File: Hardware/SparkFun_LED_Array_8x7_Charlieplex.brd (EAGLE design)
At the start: 27.9 x 43.2 mm, 76 parts

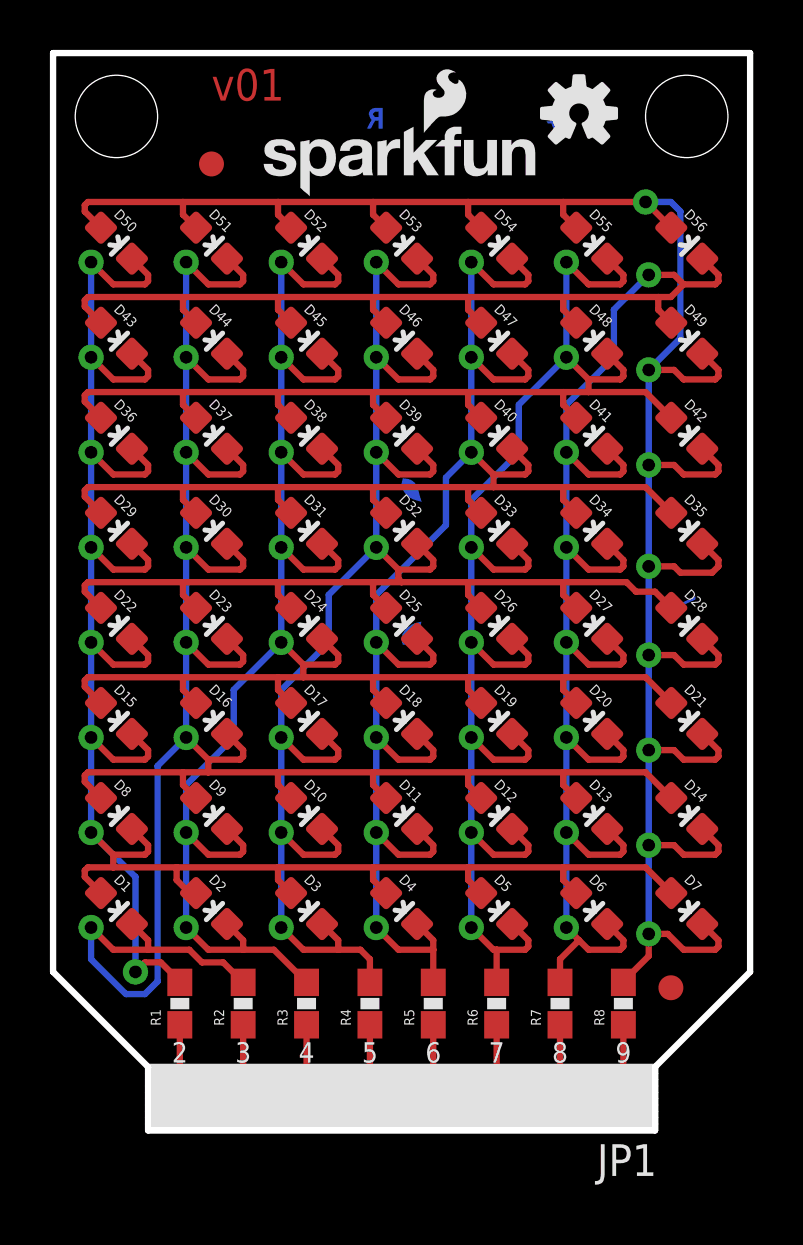
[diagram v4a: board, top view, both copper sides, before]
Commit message: Flipped all silk screen on bottom of board. Switched top and bottom silk pin numbers. Flipped order of pin numbers to line up with the Interactive Badge.
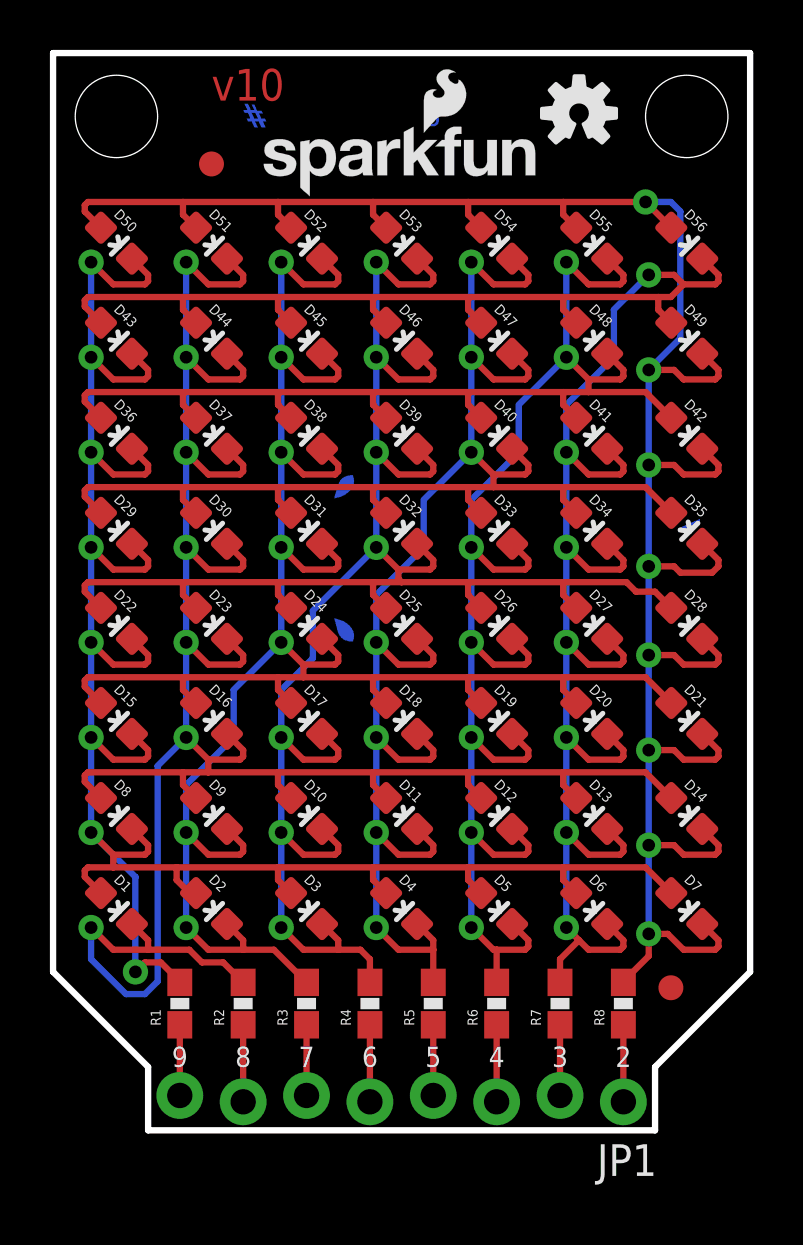
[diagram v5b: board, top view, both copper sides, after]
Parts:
- moved U$3 22.5 mm to (25.0, 11.9), turned to 90 degrees
- moved U$4 22.3 mm to (4.45, 15.7), turned to 90 degrees
- moved U$6 12.9 mm to (7.62, 41.1), turned to 180 degrees

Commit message: Changed pin numbers to letters (A-H). Changed revision to v11.
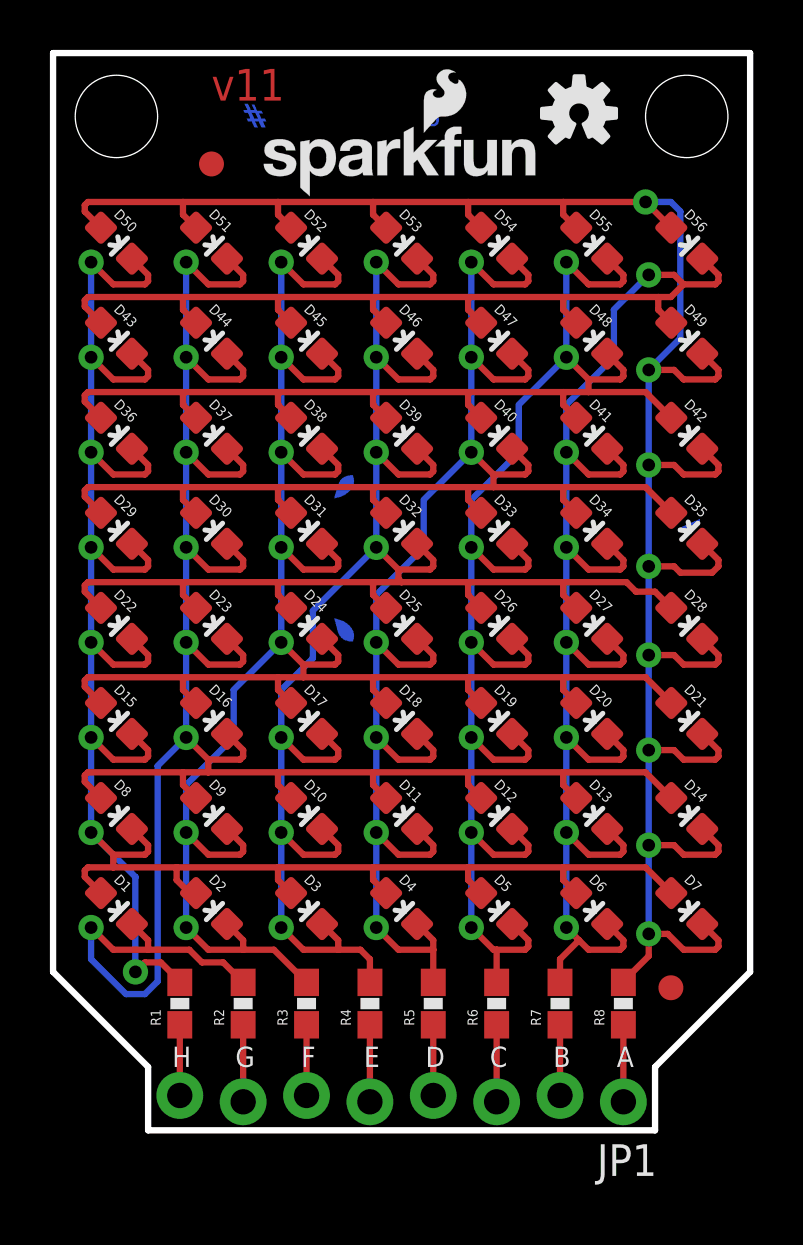
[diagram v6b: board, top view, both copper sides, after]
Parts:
- R1, R2, R3, R4, R5, R6, R7, R8: value 33 -> 82
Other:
- board text added: "A"
- board text added: "B"
- board text added: "C"
- board text added: "D"
- board text added: "E"
- board text added: "F"
- board text added: "G"
- board text added: "H"
- board text removed: "2"
- board text removed: "3"
- board text removed: "4"
- board text removed: "5"
- board text removed: "6"
- board text removed: "7"
- board text removed: "8"
- board text removed: "9"

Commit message: Swapped resistors for 82 Ohm. Made link and hashtag larger on silk.
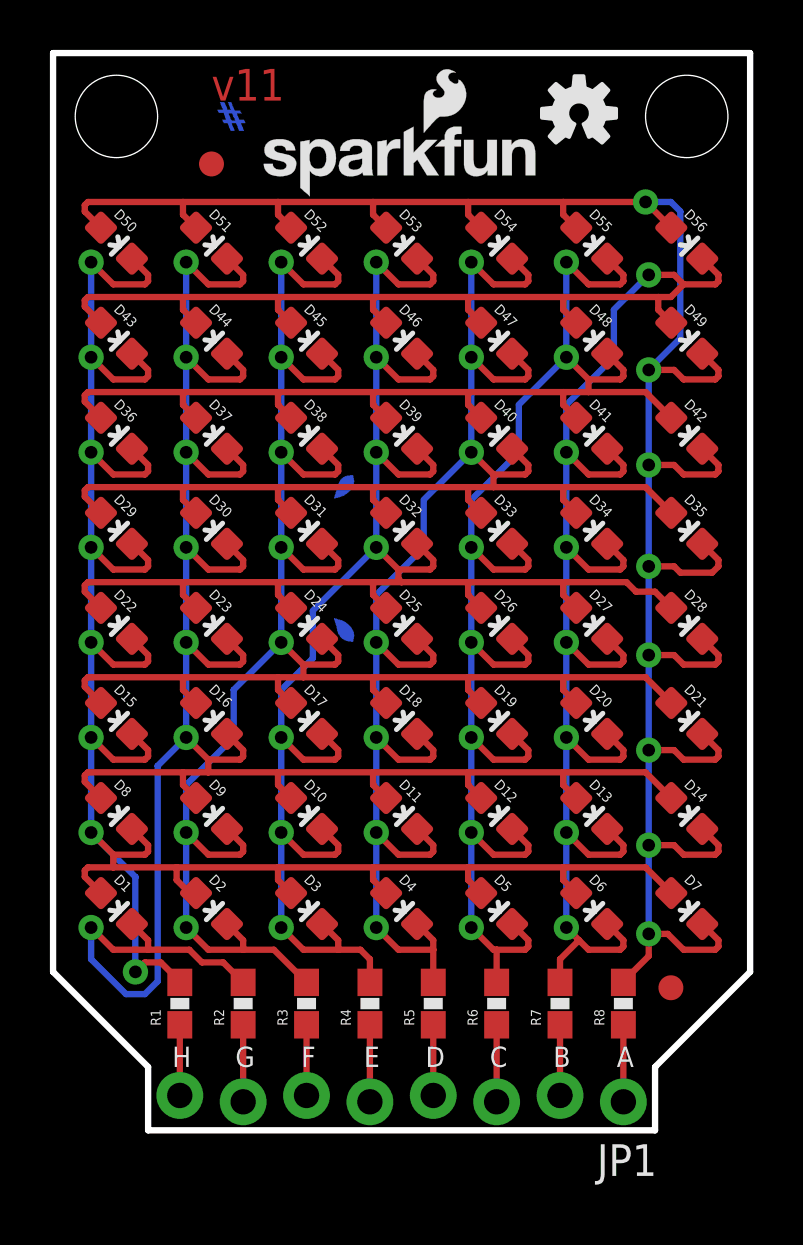
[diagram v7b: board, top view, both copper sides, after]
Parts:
- moved U$3 5.09 mm to (24.8, 6.86)
- moved U$6 1.04 mm to (6.58, 41.2)
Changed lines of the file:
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@@
 <setting verticaltext="up"/>
 </settings>
-<grid distance="0.01" unitdist="inch" unit="inch" style="dots" multiple="1" display="yes" altdistance="0.005" altunitdist="inch" altunit="inch"/>
+<grid distance="0.05" unitdist="inch" unit="inch" style="dots" multiple="1" display="yes" altdistance="0.005" altunitdist="inch" altunit="inch"/>
 <layers>
 <layer number="1" name="Top" color="4" fill="1" visible="yes" active="yes"/>
 <layer number="2" name="Route2" color="1" fill="3" visible="no" active="yes"/>
 <layer number="15" name="Route15" color="4" fill="6" visible="no" active="yes"/>
-<layer number="16" name="Bottom" color="1" fill="1" visible="no" active="yes"/>
+<layer number="16" name="Bottom" color="1" fill="1" visible="yes" active="yes"/>
 <layer number="17" name="Pads" color="2" fill="1" visible="yes" active="yes"/>
 <layer number="18" name="Vias" color="2" fill="1" visible="yes" active="yes"/>
@@
 <layer number="20" name="Dimension" color="15" fill="1" visible="yes" active="yes"/>
 <layer number="21" name="tPlace" color="16" fill="1" visible="yes" active="yes"/>
-<layer number="22" name="bPlace" color="14" fill="1" visible="no" active="yes"/>
+<layer number="22" name="bPlace" color="14" fill="1" visible="yes" active="yes"/>
 <layer number="23" name="tOrigins" color="15" fill="1" visible="yes" active="yes"/>
-<layer number="24" name="bOrigins" color="15" fill="1" visible="no" active="yes"/>
+<layer number="24" name="bOrigins" color="15" fill="1" visible="yes" active="yes"/>
 <layer number="25" name="tNames" color="7" fill="1" visible="no" active="yes"/>
 <layer number="26" name="bNames" color="7" fill="1" visible="no" active="yes"/>
@@
 <layer number="43" name="vRestrict" color="2" fill="10" visible="no" active="yes"/>
 <layer number="44" name="Drills" color="7" fill="1" visible="no" active="yes"/>
-<layer number="45" name="Holes" color="7" fill="1" visible="no" active="yes"/>
+<layer number="45" name="Holes" color="7" fill="1" visible="yes" active="yes"/>
 <layer number="46" name="Milling" color="3" fill="1" visible="no" active="yes"/>
-<layer number="47" name="Measures" color="7" fill="1" visible="no" active="yes"/>
-<layer number="51" name="tDocu" color="6" fill="1" visible="no" active="yes"/>
+<layer number="47" name="Measures" color="7" fill="1" visible="yes" active="yes"/>
+<layer number="51" name="tDocu" color="6" fill="1" visible="yes" active="yes"/>
 <layer number="52" name="bDocu" color="7" fill="1" visible="no" active="yes"/>
 <layer number="3" name="Route3" color="4" fill="3" visible="no" active="no"/>
@@
 <layer number="56" name="wert" color="7" fill="1" visible="no" active="no"/>
 <layer number="57" name="tCAD" color="7" fill="1" visible="no" active="no"/>
+<layer number="59" name="tCarbon" color="7" fill="1" visible="no" active="no"/>
+<layer number="60" name="bCarbon" color="7" fill="1" visible="no" active="no"/>
 <layer number="90" name="Modules" color="5" fill="1" visible="no" active="no"/>
 <layer number="91" name="Nets" color="2" fill="1" visible="no" active="no"/>
@@
 <layer number="127" name="_tValues" color="7" fill="1" visible="no" active="no"/>
 <layer number="128" name="_bValues" color="7" fill="1" visible="no" active="no"/>
+<layer number="129" name="Mask" color="7" fill="1" visible="no" active="no"/>
 <layer number="131" name="tAdjust" color="7" fill="1" visible="no" active="no"/>
 <layer number="132" name="bAdjust" color="7" fill="1" visible="no" active="no"/>
@@
 <dimension x1="3.7084" y1="41.8084" x2="7.62" y2="45.72" x3="8.89" y3="45.72" textsize="1.778" textratio="15" layer="47" dtype="leader" unit="inch"/>
 <text x="9.525" y="45.72" size="1.778" layer="47" ratio="15" align="center-left">0.13</text>
-<text x="5.0038" y="2.8194" size="0.8128" layer="22" font="vector" ratio="15" rot="MR0" align="bottom-center">H</text>
-<text x="7.5438" y="2.8194" size="0.8128" layer="22" font="vector" ratio="15" rot="MR0" align="bottom-center">G</text>
-<text x="10.0838" y="2.8194" size="0.8128" layer="22" font="vector" ratio="15" rot="MR0" align="bottom-center">F</text>
-<text x="12.6238" y="2.8194" size="0.8128" layer="22" font="vector" ratio="15" rot="MR0" align="bottom-center">E</text>
-<text x="15.1638" y="2.8194" size="0.8128" layer="22" font="vector" ratio="15" rot="MR0" align="bottom-center">D</text>
-<text x="17.7038" y="2.8194" size="0.8128" layer="22" font="vector" ratio="15" rot="MR0" align="bottom-center">C</text>
-<text x="20.2438" y="2.8194" size="0.8128" layer="22" font="vector" ratio="15" rot="MR0" align="bottom-center">B</text>
-<text x="22.7838" y="2.8194" size="0.8128" layer="22" font="vector" ratio="15" rot="MR0" align="bottom-center">A</text>
+<text x="5.0038" y="2.9464" size="0.8128" layer="22" font="vector" ratio="15" rot="MR0" align="bottom-center">H</text>
+<text x="7.5438" y="2.9464" size="0.8128" layer="22" font="vector" ratio="15" rot="MR0" align="bottom-center">G</text>
+<text x="10.0838" y="2.9464" size="0.8128" layer="22" font="vector" ratio="15" rot="MR0" align="bottom-center">F</text>
+<text x="12.6238" y="2.9464" size="0.8128" layer="22" font="vector" ratio="15" rot="MR0" align="bottom-center">E</text>
+<text x="15.1638" y="2.9464" size="0.8128" layer="22" font="vector" ratio="15" rot="MR0" align="bottom-center">D</text>
+<text x="17.7038" y="2.9464" size="0.8128" layer="22" font="vector" ratio="15" rot="MR0" align="bottom-center">C</text>
+<text x="20.2438" y="2.9464" size="0.8128" layer="22" font="vector" ratio="15" rot="MR0" align="bottom-center">B</text>
+<text x="22.7838" y="2.9464" size="0.8128" layer="22" font="vector" ratio="15" rot="MR0" align="bottom-center">A</text>
 <wire x1="3.81" y1="2.032" x2="24.13" y2="2.032" width="0.254" layer="22"/>
 <wire x1="3.81" y1="1.778" x2="24.13" y2="1.778" width="0.254" layer="22"/>
@@
 <element name="FRAME1" library="SparkFun-Aesthetics" package="CREATIVE_COMMONS" value="" x="-11.43" y="-26.67" smashed="yes">
 <attribute name="VERSION" value="v11" x="6.35" y="41.275" size="1.27" layer="1" font="vector" ratio="15" rot="SR0"/>
-<attribute name="DESIGNER" value="Shawn Hymel" x="15.24" y="-26.67" size="1.778" layer="51"/>
+<attribute name="DESIGNER" value="Shawn Hymel" x="20.32" y="-26.67" size="1.778" layer="51"/>
 </element>
 <element name="LOGO2" library="SparkFun-Aesthetics" package="OSHW-LOGO-S" value="OSHW-LOGOS" x="21.082" y="40.767"/>
@@
 <element name="JP1" library="SparkFun-Connectors" package="1X08_LOCK_NO_SILK" value="" x="22.86" y="1.27" rot="R180"/>
 <element name="U$2" library="SparkFun-Aesthetics" package="DUMMY" value="BADGERHACK_LOGODUMMY" x="-31.75" y="-12.7"/>
-<element name="U$3" library="SparkFun-Aesthetics" package="BADGER_ADDRESS" value="" x="25.019" y="11.938" rot="MR90"/>
+<element name="U$3" library="SparkFun-Aesthetics" package="BADGER_ADDRESS" value="" x="24.765" y="6.858" rot="MR90"/>
 <element name="U$4" library="SparkFun-Aesthetics" package="BADGER_FACE" value="" x="4.445" y="15.748" rot="MR90"/>
-<element name="U$6" library="SparkFun-Aesthetics" package="BADGER_HASHTAG" value="" x="7.62" y="41.148" rot="MR180"/>
+<element name="U$6" library="SparkFun-Aesthetics" package="BADGER_HASHTAG" value="" x="6.5786" y="41.2242" rot="MR180"/>
 </elements>
 <signals>
